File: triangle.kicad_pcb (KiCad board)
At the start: 2 copper layers, 81 x 70 mm, 54 parts, among them J1 Conn_01x02, SW1 SW_SPST

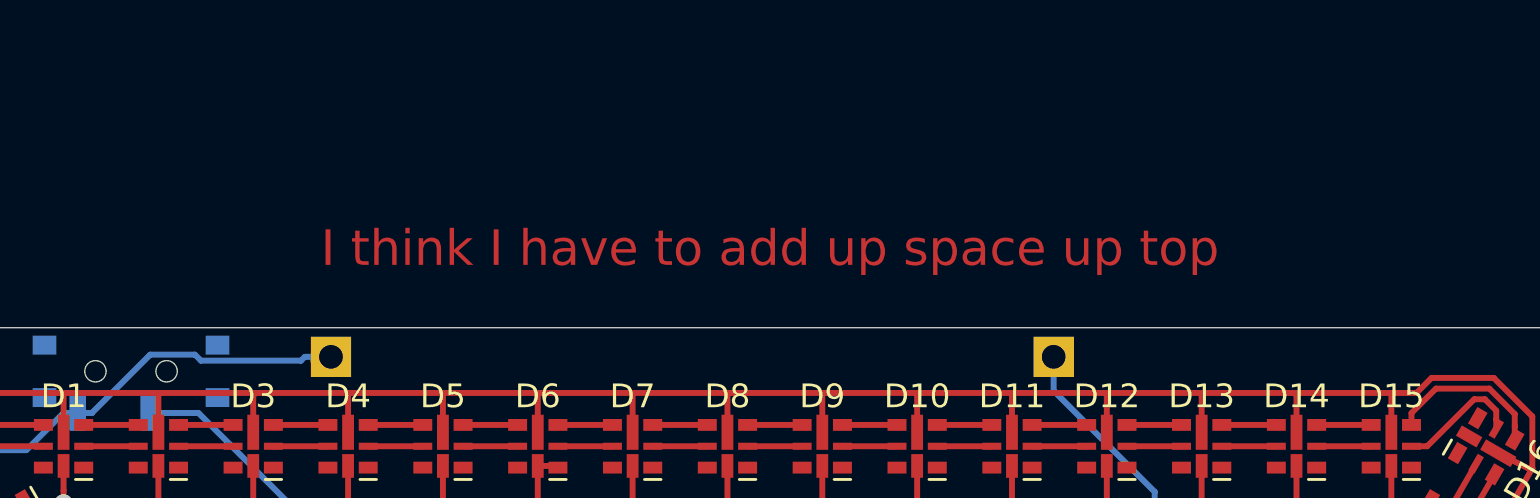
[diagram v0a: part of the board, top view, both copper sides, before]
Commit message: remove TODO label
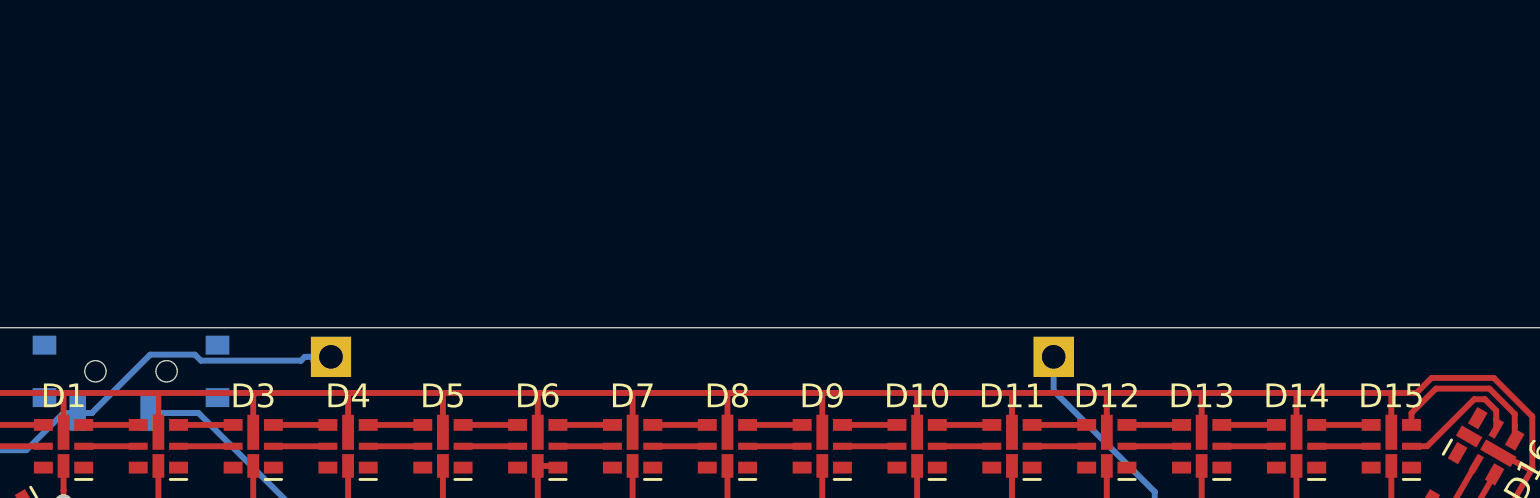
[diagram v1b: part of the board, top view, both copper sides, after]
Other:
- board text removed: "I think I have to add up space up top"
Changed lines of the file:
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@@
   (general
     (thickness 1.6)
-    (drawings 18)
+    (drawings 17)
     (tracks 425)
     (zones 0)
@@
     )
   )
-  (gr_text "I think I have to add up space up top" (at 83.7946 41.656) (layer F.Cu)
-    (effects (font (size 1.5 1.5) (thickness 0.3)))
-  )
   (gr_text ∆ (at 82.042 68.58) (layer F.SilkS)

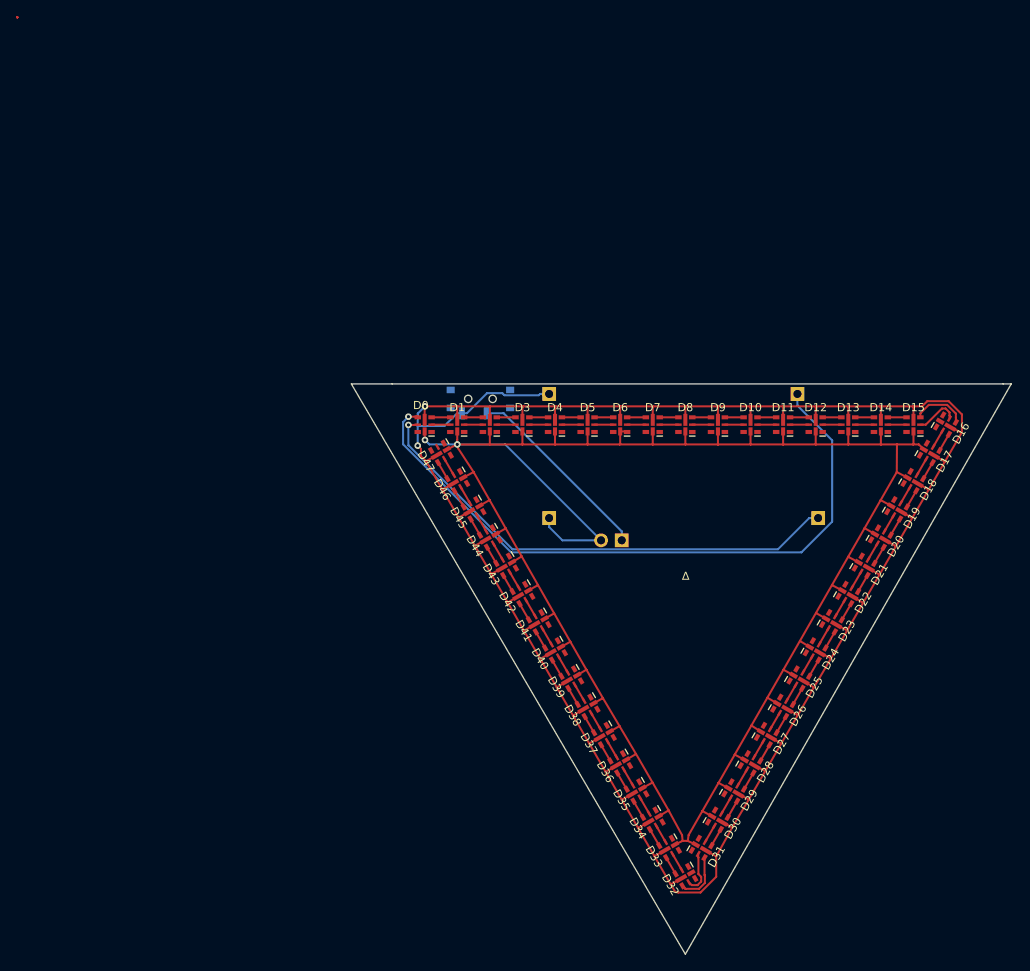
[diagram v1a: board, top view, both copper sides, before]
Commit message: add a cutout at the top center for pendant hanging
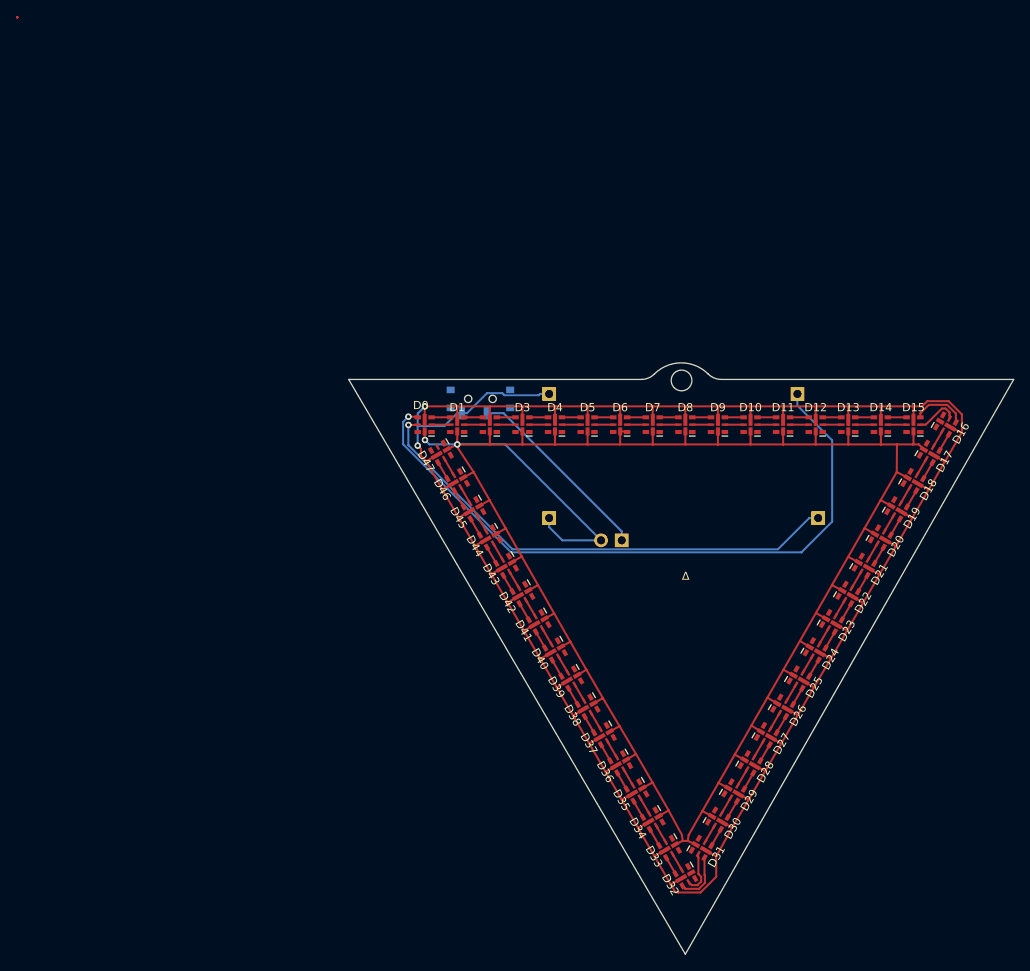
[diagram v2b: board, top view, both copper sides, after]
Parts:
- added REF**: VAL**, mechanical:Unplated_Through_Drill, F.Cu at (81.5, 44.6)
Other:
- board size 81 x 70 mm -> 81.6 x 72.6 mm
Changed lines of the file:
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@@
   (general
     (thickness 1.6)
-    (drawings 17)
+    (drawings 19)
     (tracks 425)
     (zones 0)
-    (modules 54)
+    (modules 55)
     (nets 101)
   )
@@
     (mod_text_size 1 1)
     (mod_text_width 0.15)
-    (pad_size 0.7 1.5)
-    (pad_drill 0)
+    (pad_size 2.54 2.54)
+    (pad_drill 2.54)
     (pad_to_mask_clearance 0.051)
     (solder_mask_min_width 0.25)
@@
     (add_net "Net-(D8-Pad3)")
   )
+  (module mechanical:Unplated_Through_Drill (layer F.Cu)
+    (at 81.534 44.57446)
+    (fp_text reference REF** (at 0 0.125) (layer F.Fab)
+      (effects (font (size 0.1 0.1) (thickness 0.01)))
+    )
+    (fp_text value VAL** (at 0 -0.125) (layer F.Fab)
+      (effects (font (size 0.1 0.1) (thickness 0.01)))
+    )
+    (fp_text user %R (at 0 1.85 180) (layer Eco1.User)
+      (effects (font (size 0.3 0.3) (thickness 0.03)))
+    )
+    (fp_circle (center 0 0) (end 3 0) (layer F.CrtYd) (width 0.05))
+    (fp_line (start 0 -3.1) (end 0 3.1) (layer Cmts.User) (width 0.05))
+    (fp_line (start -3.1 0) (end 3.1 0) (layer Cmts.User) (width 0.05))
+    (pad "" np_thru_hole circle (at 0 0) (size 2.54 2.54) (drill 2.54) (layers *.Cu *.Mask))
+  )
   (module Button_Switch_SMD:SW_SPDT_PCM12 (layer B.Cu)
     (at 56.8452 47.1676)
@@
     )
   )
+  (gr_line (start 86.41789 44.45) (end 122.301 44.45) (layer Edge.Cuts) (width 0.05))
+  (gr_line (start 76.581 44.45) (end 40.67302 44.45) (layer Edge.Cuts) (width 0.05))
+  (gr_arc (start 86.41789 42.164) (end 86.41789 44.45) (angle 45) (layer Edge.Cuts) (width 0.05))
+  (gr_arc (start 81.499445 47.082445) (end 78.197446 43.780446) (angle 90) (layer Edge.Cuts) (width 0.05))
+  (gr_arc (start 76.581 42.164) (end 76.581 44.45) (angle -45) (layer Edge.Cuts) (width 0.05))
   (gr_text ∆ (at 82.042 68.58) (layer F.SilkS)
     (effects (font (size 1 1) (thickness 0.15)))
@@
   (gr_line (start 99.568 62.738) (end 99.568 44.958) (layer B.SilkS) (width 0.12))
   (gr_line (start 99.568 62.738) (end 64.008 62.738) (layer B.SilkS) (width 0.12))
-  (gr_line (start 41 45) (end 46 45) (layer Edge.Cuts) (width 0.05))
-  (gr_line (start 82 115) (end 41 45) (layer Edge.Cuts) (width 0.05))
-  (gr_line (start 122 45) (end 82 115) (layer Edge.Cuts) (width 0.05))
-  (gr_line (start 121 45) (end 122 45) (layer Edge.Cuts) (width 0.05))
-  (gr_line (start 46 45) (end 121 45) (layer Edge.Cuts) (width 0.05))
+  (gr_line (start 82 115) (end 40.67302 44.45) (layer Edge.Cuts) (width 0.05))
+  (gr_line (start 122.301 44.45) (end 82 115) (layer Edge.Cuts) (width 0.05))
   (segment (start 50.85 50) (end 53.15 50) (width 0.25) (layer F.Cu) (net 1))
   (segment (start 50.85 49.1) (end 53.15 49.1) (width 0.25) (layer F.Cu) (net 2))

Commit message: tweaks to edge cuts and traces for symmetry
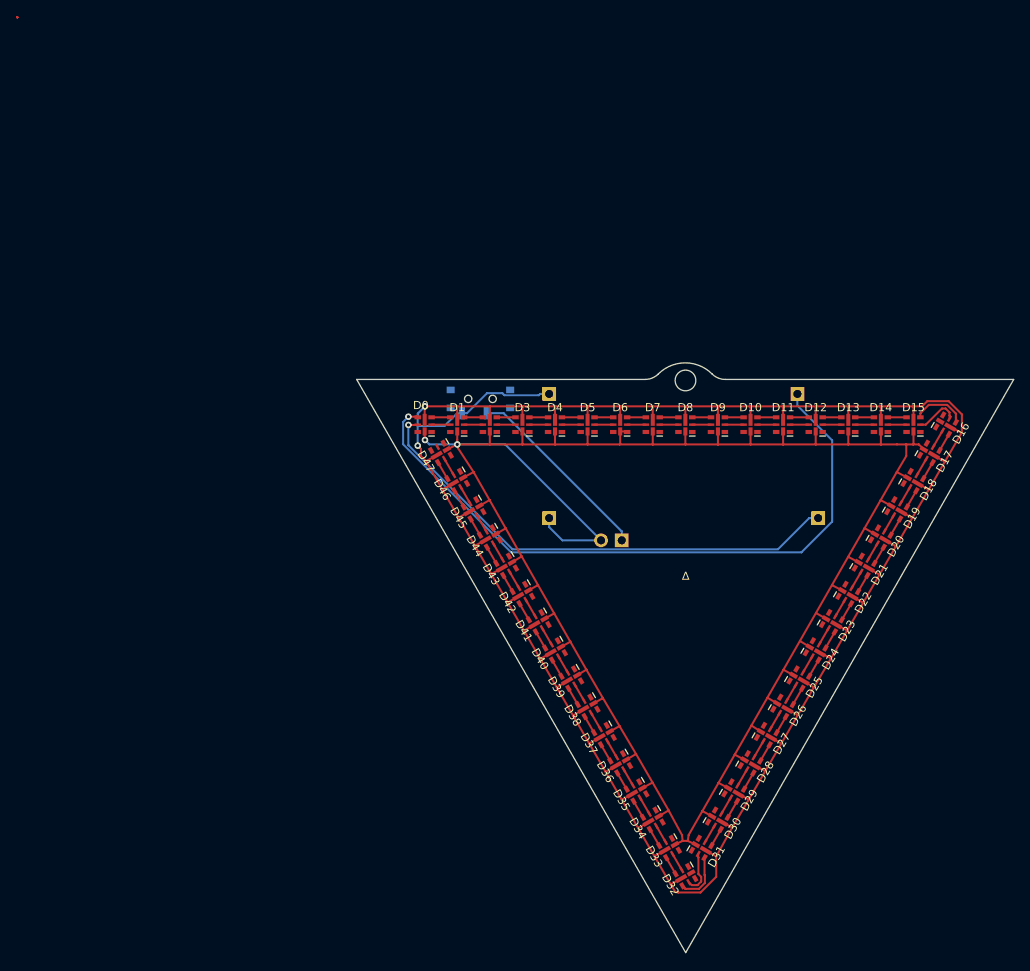
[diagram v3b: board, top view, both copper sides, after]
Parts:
- moved REF** 0.48 mm to (82.0, 44.6)
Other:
- board size 81.6 x 72.6 mm -> 80.6 x 72.4 mm
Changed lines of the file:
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@@
     (thickness 1.6)
     (drawings 19)
-    (tracks 425)
+    (tracks 427)
     (zones 0)
     (modules 55)
@@
   )
   (module mechanical:Unplated_Through_Drill (layer F.Cu)
-    (at 81.534 44.57446)
+    (at 82.0166 44.57446)
     (fp_text reference REF** (at 0 0.125) (layer F.Fab)
       (effects (font (size 0.1 0.1) (thickness 0.01)))
@@
     )
   )
-  (gr_line (start 86.41789 44.45) (end 122.301 44.45) (layer Edge.Cuts) (width 0.05))
-  (gr_line (start 76.581 44.45) (end 40.67302 44.45) (layer Edge.Cuts) (width 0.05))
-  (gr_arc (start 86.41789 42.164) (end 86.41789 44.45) (angle 45) (layer Edge.Cuts) (width 0.05))
-  (gr_arc (start 81.499445 47.082445) (end 78.197446 43.780446) (angle 90) (layer Edge.Cuts) (width 0.05))
-  (gr_arc (start 76.581 42.164) (end 76.581 44.45) (angle -45) (layer Edge.Cuts) (width 0.05))
+  (gr_line (start 82.042 114.808) (end 41.656 44.45) (layer Edge.Cuts) (width 0.05))
+  (gr_line (start 86.90049 44.45) (end 122.301 44.45) (layer Edge.Cuts) (width 0.05))
+  (gr_line (start 77.0636 44.45) (end 41.656 44.45) (layer Edge.Cuts) (width 0.05))
+  (gr_arc (start 86.90049 42.164) (end 86.90049 44.45) (angle 45) (layer Edge.Cuts) (width 0.05))
+  (gr_arc (start 81.982045 47.082445) (end 78.680046 43.780446) (angle 90) (layer Edge.Cuts) (width 0.05))
+  (gr_arc (start 77.0636 42.164) (end 77.0636 44.45) (angle -45) (layer Edge.Cuts) (width 0.05))
   (gr_text ∆ (at 82.042 68.58) (layer F.SilkS)
     (effects (font (size 1 1) (thickness 0.15)))
@@
   (gr_line (start 99.568 62.738) (end 99.568 44.958) (layer B.SilkS) (width 0.12))
   (gr_line (start 99.568 62.738) (end 64.008 62.738) (layer B.SilkS) (width 0.12))
-  (gr_line (start 82 115) (end 40.67302 44.45) (layer Edge.Cuts) (width 0.05))
-  (gr_line (start 122.301 44.45) (end 82 115) (layer Edge.Cuts) (width 0.05))
+  (gr_line (start 122.301 44.45) (end 82.042 114.808) (layer Edge.Cuts) (width 0.05))
   (segment (start 50.85 50) (end 53.15 50) (width 0.25) (layer F.Cu) (net 1))
   (segment (start 50.85 49.1) (end 53.15 49.1) (width 0.25) (layer F.Cu) (net 2))
@@
   (segment (start 109.957 52.426) (end 110.658098 52.426) (width 0.25) (layer F.Cu) (net 99))
   (segment (start 109.281199 56.513203) (end 107.95 55.8165) (width 0.25) (layer F.Cu) (net 99))
-  (segment (start 107.95 55.8165) (end 107.975 52.426) (width 0.25) (layer F.Cu) (net 99))
-  (segment (start 107.975 52.426) (end 109.957 52.426) (width 0.25) (layer F.Cu) (net 99))
   (segment (start 106.02 52.426) (end 107.975 52.426) (width 0.25) (layer F.Cu) (net 99))
   (segment (start 54.718801 56.513203) (end 56.007 55.8165) (width 0.25) (layer F.Cu) (net 99))
@@
   (segment (start 82.296 101.092) (end 82.400987 100.371487) (width 0.25) (layer F.Cu) (net 99))
   (segment (start 81.5975 100.3935) (end 81.661 101.092) (width 0.25) (layer F.Cu) (net 99))
+  (segment (start 107.95 55.8165) (end 109.1184 53.848) (width 0.25) (layer F.Cu) (net 99))
+  (segment (start 109.1184 53.848) (end 109.1184 52.4256) (width 0.25) (layer F.Cu) (net 99))
+  (segment (start 109.1184 52.4256) (end 109.957 52.426) (width 0.25) (layer F.Cu) (net 99))
+  (segment (start 107.975 52.426) (end 109.1184 52.4256) (width 0.25) (layer F.Cu) (net 99))
   (segment (start 54.5952 48.9976) (end 54.5952 48.5976) (width 0.25) (layer B.Cu) (net 100))
   (segment (start 109.15 50.9) (end 109.15 50.899998) (width 0.25) (layer F.Cu) (net 100))
